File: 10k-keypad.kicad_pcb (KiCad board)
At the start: 2 copper layers, 103.2 x 53.2 mm, 59 parts, among them J1 AVR-ISP-6, K1 SW_Push, K10 SW_Push, K2 SW_Push, K3 SW_Push, K4 SW_Push, K5 SW_Push, K6 SW_Push, K7 SW_Push, K8 SW_Push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

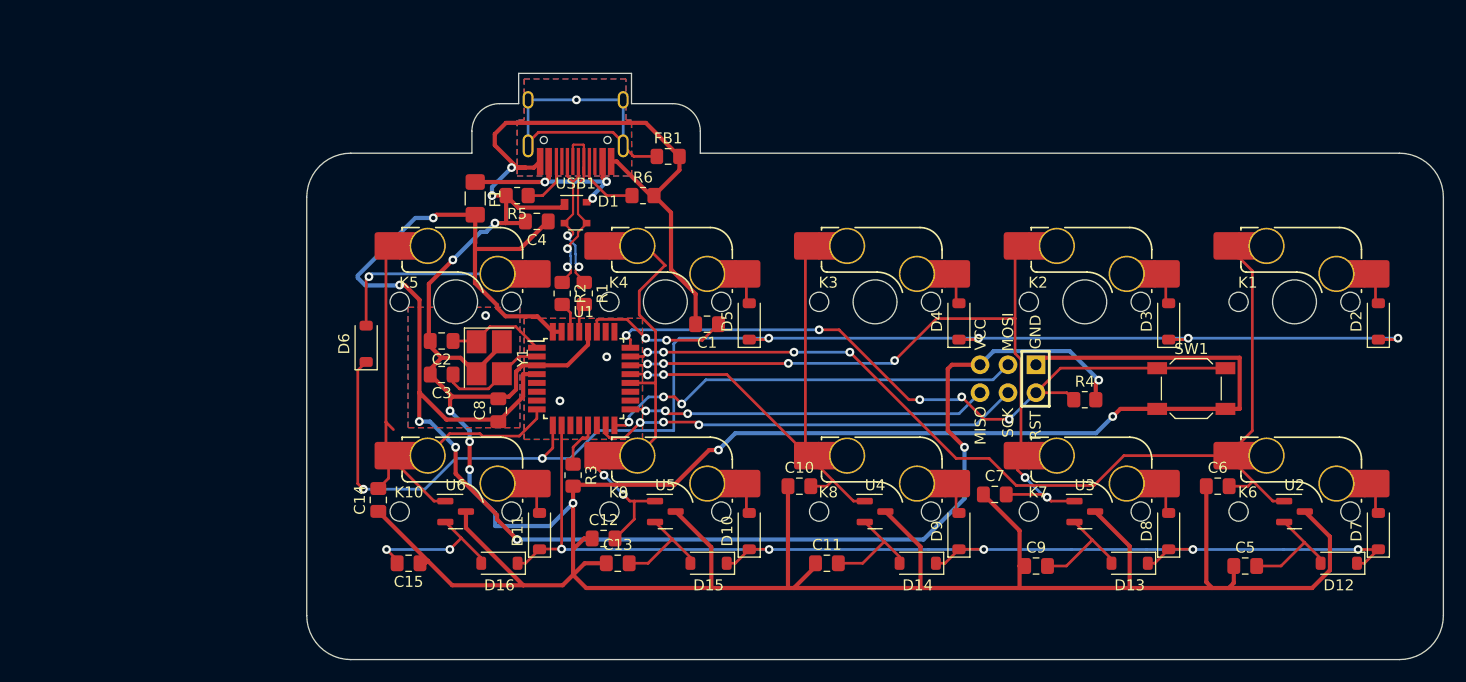
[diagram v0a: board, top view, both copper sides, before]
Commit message: fix hall sensor circuitry
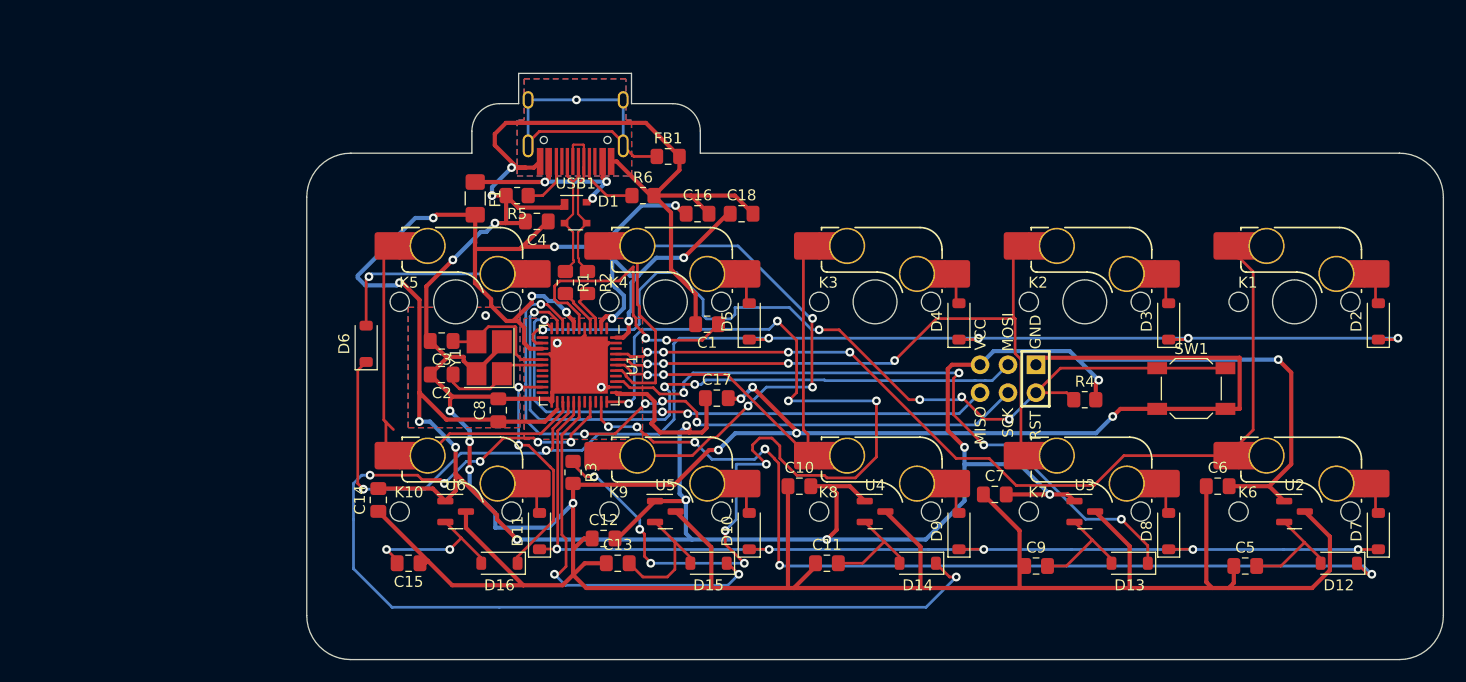
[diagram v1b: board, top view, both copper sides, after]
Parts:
- added C16: 0.1u, Capacitor_SMD:C_0805_2012Metric_Pad1.18x1.45mm_HandSolder, F.Cu at (141.5, 53.8)
- added C17: 0.1u, Capacitor_SMD:C_0805_2012Metric_Pad1.18x1.45mm_HandSolder, F.Cu at (143.2, 70.5)
- added C18: 0.1u, Capacitor_SMD:C_0805_2012Metric_Pad1.18x1.45mm_HandSolder, F.Cu at (145.5, 53.8)
- U1: value ATmega16U2-A -> ATmega32U4-M; footprint Package_QFP:TQFP-32_7x7mm_P0.8mm -> Package_DFN_QFN:QFN-44-1EP_7x7mm_P0.5mm_EP5.2x5.2mm
- moved C2 3.05 mm to (118.3, 68.4)
- moved C3 3.05 mm to (118.3, 65.3)
- moved R2 2.50 mm to (131.5, 60.0)
- moved R1 1.98 mm to (129.5, 60.0)
- moved U1 1.29 mm to (130.8, 67.5), turned to -90 degrees
- moved R3 0.25 mm to (130.2, 77.2)
- turned Y1 to 90 degrees
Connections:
- C10 pad 2: COL3 -> +5V
- C12 pad 2: COL4 -> +5V
- C14 pad 2: COL5 -> +5V
- C6 pad 2: COL1 -> +5V
- C7 pad 2: COL2 -> +5V
- D12 pad 1: ROW2 -> HALL1
- D13 pad 1: ROW2 -> HALL2
- D14 pad 1: ROW2 -> HALL3
- D15 pad 1: ROW2 -> HALL4
- D16 pad 1: ROW2 -> HALL5
- R3 pad 1: Net-(U1-~{HWB}/PD7) -> Net-(U1-~{HWB}/PE2)
- U1 pad 1: XTAL1 -> unconnected-(U1-PE6-Pad1)
- U1 pad 10: ROW2 -> MOSI
- U1 pad 11: unconnected-(U1-PD5-Pad11) -> MISO
- U1 pad 13: Net-(U1-~{HWB}/PD7) -> RESET
- U1 pad 14: unconnected-(U1-PB0-Pad14) -> +5V
- U1 pad 15: SCK -> GND
- U1 pad 16: MOSI -> XTAL2
- U1 pad 17: MISO -> XTAL1
- U1 pad 2: XTAL2 -> +5V
- U1 pad 20: COL4 -> unconnected-(U1-PD2-Pad20)
- U1 pad 21: COL3 -> HALL5
- U1 pad 22: COL2 -> unconnected-(U1-PD5-Pad22)
- U1 pad 23: COL1 -> GND
- U1 pad 24: RESET -> +5V
- U1 pad 25: unconnected-(U1-PC5-Pad25) -> COL5
- U1 pad 26: unconnected-(U1-PC4-Pad26) -> ROW1
- U1 pad 27: Net-(U1-UCAP) -> ROW2
- U1 pad 28: GND -> HALL4
- U1 pad 29: Net-(U1-D+) -> unconnected-(U1-PB5-Pad29)
- U1 pad 3: GND -> Net-(U1-D-)
- U1 pad 30: Net-(U1-D-) -> HALL3
- U1 pad 31: +5V -> unconnected-(U1-PC6-Pad31)
- U1 pad 32: +5V -> HALL1
- U1 pad 4: +5V -> Net-(U1-D+)
- U1 pad 5: unconnected-(U1-PC2-Pad5) -> GND
- U1 pad 6: unconnected-(U1-PD0-Pad6) -> Net-(U1-UCAP)
- U1 pad 7: unconnected-(U1-PD1-Pad7) -> +5V
- U1 pad 8: COL5 -> unconnected-(U1-PB0-Pad8)
- U1 pad 9: ROW1 -> SCK
- U2 pad 1: COL1 -> +5V
- U3 pad 1: COL2 -> +5V
- U4 pad 1: COL3 -> +5V
- U5 pad 1: COL4 -> +5V
- U6 pad 1: COL5 -> +5V
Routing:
- net +5V: track 155.8 -> 319.0 mm, vias 7 -> 19
- net HALL3: track 0.00 -> 94.2 mm, vias 0 -> 6
- net Net-(U1-~{HWB}/PE2): track 0.00 -> 93.9 mm, vias 0 -> 10
- net HALL1: track 0.00 -> 85.4 mm, vias 0 -> 6
- net HALL2: track 0.00 -> 61.2 mm, vias 0 -> 4
- net HALL4: track 0.00 -> 36.2 mm, vias 0 -> 2
- net GND: track 396.7 -> 429.1 mm, vias 13 -> 16
- net COL4: track 40.4 -> 66.3 mm, vias 2 -> 3
- net SCK: track 39.4 -> 63.1 mm, vias 3 -> 5
- net MOSI: track 38.9 -> 60.5 mm
- net HALL5: track 0.00 -> 21.3 mm, vias 0 -> 2
- net MISO: track 32.7 -> 50.9 mm
- net RESET: track 65.1 -> 82.1 mm
- net Net-(U1-UCAP): track 13.5 -> 27.4 mm
- net ROW2: track 106.4 -> 96.4 mm
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
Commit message: fix schematic, gerbers
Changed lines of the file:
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@@
     (fp_line (start 3.5 3.5) (end -3.5 3.5)
       (stroke (width 0.1) (type solid)) (layer "F.Fab"))
-    (pad "" smd roundrect (at -1.95 -1.95 270) (size 1.05 1.05) (layers "F.Paste") (roundrect_rratio 0.238095))
-    (pad "" smd roundrect (at -1.95 -0.65 270) (size 1.05 1.05) (layers "F.Paste") (roundrect_rratio 0.238095))
-    (pad "" smd roundrect (at -1.95 0.65 270) (size 1.05 1.05) (layers "F.Paste") (roundrect_rratio 0.238095))
-    (pad "" smd roundrect (at -1.95 1.95 270) (size 1.05 1.05) (layers "F.Paste") (roundrect_rratio 0.238095))
-    (pad "" smd roundrect (at -0.65 -1.95 270) (size 1.05 1.05) (layers "F.Paste") (roundrect_rratio 0.238095))
-    (pad "" smd roundrect (at -0.65 -0.65 270) (size 1.05 1.05) (layers "F.Paste") (roundrect_rratio 0.238095))
-    (pad "" smd roundrect (at -0.65 0.65 270) (size 1.05 1.05) (layers "F.Paste") (roundrect_rratio 0.238095))
-    (pad "" smd roundrect (at -0.65 1.95 270) (size 1.05 1.05) (layers "F.Paste") (roundrect_rratio 0.238095))
-    (pad "" smd roundrect (at 0.65 -1.95 270) (size 1.05 1.05) (layers "F.Paste") (roundrect_rratio 0.238095))
-    (pad "" smd roundrect (at 0.65 -0.65 270) (size 1.05 1.05) (layers "F.Paste") (roundrect_rratio 0.238095))
-    (pad "" smd roundrect (at 0.65 0.65 270) (size 1.05 1.05) (layers "F.Paste") (roundrect_rratio 0.238095))
-    (pad "" smd roundrect (at 0.65 1.95 270) (size 1.05 1.05) (layers "F.Paste") (roundrect_rratio 0.238095))
-    (pad "" smd roundrect (at 1.95 -1.95 270) (size 1.05 1.05) (layers "F.Paste") (roundrect_rratio 0.238095))
-    (pad "" smd roundrect (at 1.95 -0.65 270) (size 1.05 1.05) (layers "F.Paste") (roundrect_rratio 0.238095))
-    (pad "" smd roundrect (at 1.95 0.65 270) (size 1.05 1.05) (layers "F.Paste") (roundrect_rratio 0.238095))
-    (pad "" smd roundrect (at 1.95 1.95 270) (size 1.05 1.05) (layers "F.Paste") (roundrect_rratio 0.238095))
+    (pad "" smd roundrect (at -1.95 -1.95 270) (size 1.05 1.05) (layers "F.Paste") (roundrect_rratio 0.2380952381))
+    (pad "" smd roundrect (at -1.95 -0.65 270) (size 1.05 1.05) (layers "F.Paste") (roundrect_rratio 0.2380952381))
+    (pad "" smd roundrect (at -1.95 0.65 270) (size 1.05 1.05) (layers "F.Paste") (roundrect_rratio 0.2380952381))
+    (pad "" smd roundrect (at -1.95 1.95 270) (size 1.05 1.05) (layers "F.Paste") (roundrect_rratio 0.2380952381))
+    (pad "" smd roundrect (at -0.65 -1.95 270) (size 1.05 1.05) (layers "F.Paste") (roundrect_rratio 0.2380952381))
+    (pad "" smd roundrect (at -0.65 -0.65 270) (size 1.05 1.05) (layers "F.Paste") (roundrect_rratio 0.2380952381))
+    (pad "" smd roundrect (at -0.65 0.65 270) (size 1.05 1.05) (layers "F.Paste") (roundrect_rratio 0.2380952381))
+    (pad "" smd roundrect (at -0.65 1.95 270) (size 1.05 1.05) (layers "F.Paste") (roundrect_rratio 0.2380952381))
+    (pad "" smd roundrect (at 0.65 -1.95 270) (size 1.05 1.05) (layers "F.Paste") (roundrect_rratio 0.2380952381))
+    (pad "" smd roundrect (at 0.65 -0.65 270) (size 1.05 1.05) (layers "F.Paste") (roundrect_rratio 0.2380952381))
+    (pad "" smd roundrect (at 0.65 0.65 270) (size 1.05 1.05) (layers "F.Paste") (roundrect_rratio 0.2380952381))
+    (pad "" smd roundrect (at 0.65 1.95 270) (size 1.05 1.05) (layers "F.Paste") (roundrect_rratio 0.2380952381))
+    (pad "" smd roundrect (at 1.95 -1.95 270) (size 1.05 1.05) (layers "F.Paste") (roundrect_rratio 0.2380952381))
+    (pad "" smd roundrect (at 1.95 -0.65 270) (size 1.05 1.05) (layers "F.Paste") (roundrect_rratio 0.2380952381))
+    (pad "" smd roundrect (at 1.95 0.65 270) (size 1.05 1.05) (layers "F.Paste") (roundrect_rratio 0.2380952381))
+    (pad "" smd roundrect (at 1.95 1.95 270) (size 1.05 1.05) (layers "F.Paste") (roundrect_rratio 0.2380952381))
     (pad "1" smd roundrect (at -3.3375 -2.5 270) (size 1.075 0.25) (layers "F.Cu" "F.Paste" "F.Mask") (roundrect_rratio 0.25)
       (net 43 "unconnected-(U1-PE6-Pad1)") (pinfunction "PE6") (pintype "bidirectional+no_connect"))
@@
     (fp_line (start 1 0.625) (end -1 0.625)
       (stroke (width 0.1) (type solid)) (layer "F.Fab"))
-    (pad "1" smd roundrect (at -1.0375 0) (size 1.175 1.45) (layers "F.Cu" "F.Paste" "F.Mask") (roundrect_rratio 0.212766)
+    (pad "1" smd roundrect (at -1.0375 0) (size 1.175 1.45) (layers "F.Cu" "F.Paste" "F.Mask") (roundrect_rratio 0.2127659574)
       (net 5 "+5V") (pintype "passive"))
-    (pad "2" smd roundrect (at 1.0375 0) (size 1.175 1.45) (layers "F.Cu" "F.Paste" "F.Mask") (roundrect_rratio 0.212766)
+    (pad "2" smd roundrect (at 1.0375 0) (size 1.175 1.45) (layers "F.Cu" "F.Paste" "F.Mask") (roundrect_rratio 0.2127659574)
       (net 2 "GND") (pintype "passive"))
     (model "${KICAD6_3DMODEL_DIR}/Capacitor_SMD.3dshapes/C_0805_2012Metric.wrl"
@@
     (fp_line (start 1 0.625) (end -1 0.625)
       (stroke (width 0.1) (type solid)) (layer "F.Fab"))
-    (pad "1" smd roundrect (at -1.0375 0) (size 1.175 1.45) (layers "F.Cu" "F.Paste" "F.Mask") (roundrect_rratio 0.212766)
+    (pad "1" smd roundrect (at -1.0375 0) (size 1.175 1.45) (layers "F.Cu" "F.Paste" "F.Mask") (roundrect_rratio 0.2127659574)
       (net 5 "+5V") (pintype "passive"))
-    (pad "2" smd roundrect (at 1.0375 0) (size 1.175 1.45) (layers "F.Cu" "F.Paste" "F.Mask") (roundrect_rratio 0.212766)
+    (pad "2" smd roundrect (at 1.0375 0) (size 1.175 1.45) (layers "F.Cu" "F.Paste" "F.Mask") (roundrect_rratio 0.2127659574)
       (net 2 "GND") (pintype "passive"))
     (model "${KICAD6_3DMODEL_DIR}/Capacitor_SMD.3dshapes/C_0805_2012Metric.wrl"
@@
     (fp_line (start 1 0.625) (end -1 0.625)
       (stroke (width 0.1) (type solid)) (layer "F.Fab"))
-    (pad "1" smd roundrect (at -1.0375 0) (size 1.175 1.45) (layers "F.Cu" "F.Paste" "F.Mask") (roundrect_rratio 0.212766)
+    (pad "1" smd roundrect (at -1.0375 0) (size 1.175 1.45) (layers "F.Cu" "F.Paste" "F.Mask") (roundrect_rratio 0.2127659574)
       (net 5 "+5V") (pintype "passive"))
-    (pad "2" smd roundrect (at 1.0375 0) (size 1.175 1.45) (layers "F.Cu" "F.Paste" "F.Mask") (roundrect_rratio 0.212766)
+    (pad "2" smd roundrect (at 1.0375 0) (size 1.175 1.45) (layers "F.Cu" "F.Paste" "F.Mask") (roundrect_rratio 0.2127659574)
       (net 2 "GND") (pintype "passive"))
     (model "${KICAD6_3DMODEL_DIR}/Capacitor_SMD.3dshapes/C_0805_2012Metric.wrl"

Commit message: fix pcb labels
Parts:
- C16, C17, C18, C8: value 0.1u -> 100n
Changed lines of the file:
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@@
         (effects (font (size 1 1) (thickness 0.15)))
     )
-    (fp_text value "0.1u" (at 0 1.68 90) (layer "F.Fab")
+    (fp_text value "100n" (at 0 1.68 90) (layer "F.Fab")
         (effects (font (size 1 1) (thickness 0.15)))
     )
@@
         (effects (font (size 1 1) (thickness 0.15)))
     )
-    (fp_text value "0.1u" (at 0 1.68) (layer "F.Fab")
+    (fp_text value "100n" (at 0 1.68) (layer "F.Fab")
         (effects (font (size 1 1) (thickness 0.15)))
     )
@@
         (effects (font (size 1 1) (thickness 0.15)))
     )
-    (fp_text value "0.1u" (at 0 1.68) (layer "F.Fab")
+    (fp_text value "100n" (at 0 1.68) (layer "F.Fab")
         (effects (font (size 1 1) (thickness 0.15)))
     )
@@
         (effects (font (size 1 1) (thickness 0.15)))
     )
-    (fp_text value "0.1u" (at 0 1.68) (layer "F.Fab")
-        (effects (font (size 1 1) (thickness 0.15)))
-    )
+    (fp_text value "100n" (at 0 1.68) (layer "F.Fab")
+        (effects (font (size 1 1) (thickness 0.15)))
+    )

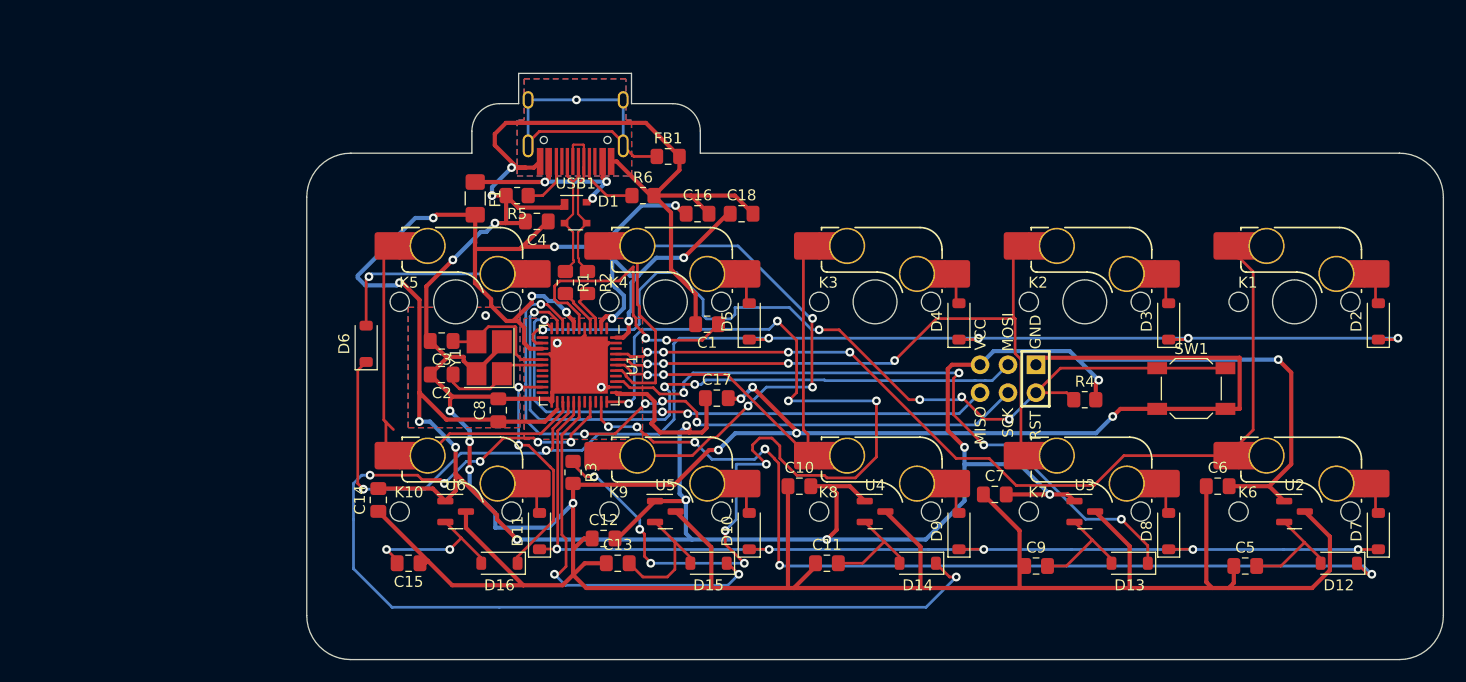
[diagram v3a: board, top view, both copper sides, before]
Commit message: redo all routing, remove unused footprint
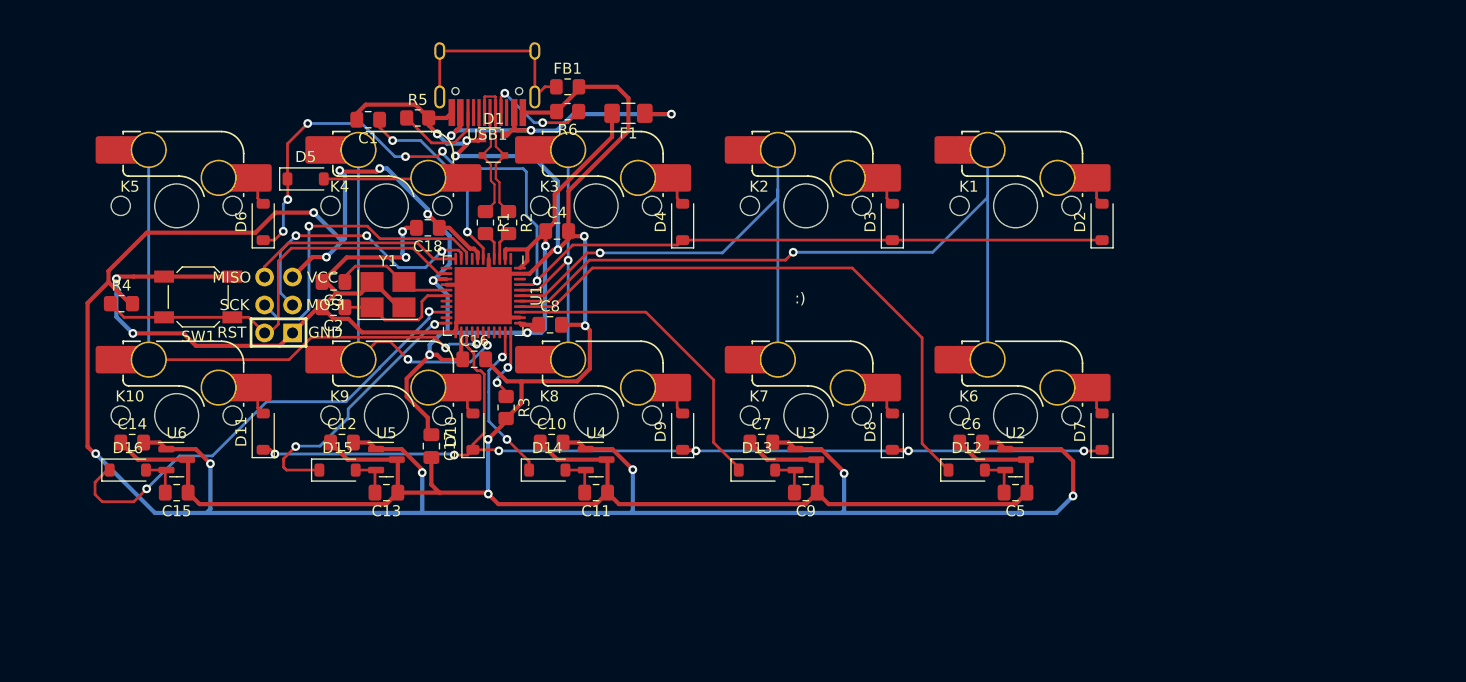
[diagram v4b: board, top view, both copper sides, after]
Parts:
- K10, K6, K7, K8, K9: footprint Hall:SW_MX_HS_CPG151101S11_1u_no_center_piece -> marbastlib-mx:SW_MX_HS_CPG151101S11_1u
- moved SW1 90.6 mm to (96.1, 61.3), turned to 180 degrees
- moved R4 87.9 mm to (89.2, 61.9)
- moved J1 66.6 mm to (103.4, 62.0), turned to 0 degrees
- moved D5 42.3 mm to (105.9, 50.6), turned to 0 degrees
- moved C1 36.0 mm to (111.6, 45.2)
- moved D13 34.9 mm to (146.9, 77.0), turned to 0 degrees
- moved D12 34.8 mm to (165.9, 77.0), turned to 0 degrees
- moved D16 34.8 mm to (89.7, 77.0), turned to 0 degrees
- moved D15 34.7 mm to (108.8, 77.0), turned to 0 degrees
- moved D14 34.7 mm to (127.8, 77.0), turned to 0 degrees
- moved C18 28.5 mm to (117.0, 55.0), turned to 180 degrees
- moved K1 26.8 mm to (170.4, 53.0)
- moved K6 26.8 mm to (170.4, 72.1)
- moved K4 26.8 mm to (113.2, 53.0)
- moved K9 26.8 mm to (113.2, 72.1)
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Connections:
- U1 pad 20: unconnected-(U1-PD2-Pad20) -> HALL5
- U1 pad 21: HALL5 -> unconnected-(U1-PD3-Pad21)
- U1 pad 22: unconnected-(U1-PD5-Pad22) -> HALL4
- U1 pad 25: COL5 -> ROW2
- U1 pad 26: ROW1 -> COL5
- U1 pad 27: ROW2 -> unconnected-(U1-PD7-Pad27)
- U1 pad 28: HALL4 -> COL4
- U1 pad 30: HALL3 -> unconnected-(U1-PB6-Pad30)
- U1 pad 32: HALL1 -> HALL3
- U1 pad 37: unconnected-(U1-PF6-Pad37) -> HALL1
- U1 pad 38: COL4 -> COL1
- U1 pad 39: COL3 -> COL2
- U1 pad 40: COL2 -> COL3
- U1 pad 41: COL1 -> ROW1
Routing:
- net GND: track 429.1 -> 335.9 mm, vias 16 -> 12
- net Net-(U1-~{HWB}/PE2): track 93.9 -> 6.68 mm, vias 10 -> 2
- net HALL3: track 94.2 -> 14.6 mm, vias 6 -> 2
- net RESET: track 82.1 -> 39.1 mm, vias 5 -> 0
- net MOSI: track 60.5 -> 24.8 mm
- net SCK: track 63.1 -> 28.4 mm, vias 5 -> 1
- net COL4: track 66.3 -> 34.2 mm, vias 3 -> 2
- net HALL2: track 61.2 -> 29.3 mm, vias 4 -> 0
- net HALL1: track 85.4 -> 53.6 mm, vias 6 -> 0
- net MISO: track 50.9 -> 19.8 mm, vias 3 -> 0
- net ROW1: track 128.6 -> 100.1 mm
- net +5V: track 319.0 -> 296.8 mm, vias 19 -> 15
- net HALL5: track 21.3 -> 42.7 mm
- net Net-(D6-A): track 20.7 -> 2.56 mm, vias 1 -> 0
- net COL1: track 82.9 -> 65.5 mm, vias 4 -> 1
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- removed copper zone on B.Cu, net Earth
- removed copper zone on F.Cu, net Earth
- removed copper zone on B.Cu, net GND
- removed copper zone on F.Cu, net GND
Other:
- board outline removed
- board text added: ":)"
